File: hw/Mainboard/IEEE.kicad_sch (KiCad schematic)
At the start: 26 parts, among them J10 IEEE_HEADER, J11 IEEE, U14 74LS245, U15 SN74LS07, U16 SN74LS07, U17 74LS245, U18 SN74LS07

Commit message: hw: 25x2 header (wip)
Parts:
- renumbered J10 to J11, J11 to J12
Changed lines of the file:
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@@
   (symbol (lib_id "Retrocomputing:CBM_PET_IEEE_Conn_02x12_Card_Edge") (at 238.76 119.38 0) (unit 1)
     (in_bom yes) (on_board yes)
-    (property "Reference" "J11" (id 0) (at 240.03 101.1682 0))
+    (property "Reference" "J12" (id 0) (at 240.03 101.1682 0))
     (property "Value" "IEEE" (id 1) (at 240.03 103.4796 0))
     (property "Footprint" "Retrocomputing:CBM_PET_IEEE_EDGE_CON_24P" (id 2) (at 238.76 119.38 0)
@@
   (symbol (lib_id "PET:PD_GND") (at 204.47 44.45 0) (unit 1)
     (in_bom yes) (on_board yes) (fields_autoplaced)
-    (property "Reference" "#PWR090" (id 0) (at 204.47 50.8 0)
+    (property "Reference" "#PWR092" (id 0) (at 204.47 50.8 0)
       (effects (font (size 1.27 1.27)) hide)
     )
@@
   (symbol (lib_id "power:GND") (at 194.31 147.32 0) (unit 1)
     (in_bom yes) (on_board yes)
-    (property "Reference" "#PWR099" (id 0) (at 194.31 153.67 0)
+    (property "Reference" "#PWR0101" (id 0) (at 194.31 153.67 0)
       (effects (font (size 1.27 1.27)) hide)
     )
@@
   (symbol (lib_id "Connector_Generic:Conn_02x09_Odd_Even") (at 210.82 34.29 0) (mirror x) (unit 1)
     (in_bom yes) (on_board yes) (fields_autoplaced)
-    (property "Reference" "J10" (id 0) (at 212.09 17.78 0))
+    (property "Reference" "J11" (id 0) (at 212.09 17.78 0))
     (property "Value" "IEEE_HEADER" (id 1) (at 212.09 20.32 0))
     (property "Footprint" "Connector_PinHeader_2.54mm:PinHeader_2x09_P2.54mm_Vertical" (id 2) (at 210.82 34.29 0)
@@
   (symbol (lib_id "power:+5V") (at 67.31 130.81 0) (unit 1)
     (in_bom yes) (on_board yes) (fields_autoplaced)
-    (property "Reference" "#PWR095" (id 0) (at 67.31 134.62 0)
+    (property "Reference" "#PWR097" (id 0) (at 67.31 134.62 0)
       (effects (font (size 1.27 1.27)) hide)
     )
@@
   (symbol (lib_id "power:GND") (at 128.27 71.12 0) (unit 1)
     (in_bom yes) (on_board yes)
-    (property "Reference" "#PWR093" (id 0) (at 128.27 77.47 0)
+    (property "Reference" "#PWR095" (id 0) (at 128.27 77.47 0)
       (effects (font (size 1.27 1.27)) hide)
     )
@@
   (symbol (lib_id "PET:PD_GND") (at 219.71 44.45 0) (unit 1)
     (in_bom yes) (on_board yes) (fields_autoplaced)
-    (property "Reference" "#PWR091" (id 0) (at 219.71 50.8 0)
+    (property "Reference" "#PWR093" (id 0) (at 219.71 50.8 0)
       (effects (font (size 1.27 1.27)) hide)
     )
@@
   (symbol (lib_id "PET:PD_GND") (at 247.65 135.89 0) (unit 1)
     (in_bom yes) (on_board yes) (fields_autoplaced)
-    (property "Reference" "#PWR097" (id 0) (at 247.65 142.24 0)
+    (property "Reference" "#PWR099" (id 0) (at 247.65 142.24 0)
       (effects (font (size 1.27 1.27)) hide)
     )
@@
   (symbol (lib_id "power:GND") (at 64.77 193.04 0) (unit 1)
     (in_bom yes) (on_board yes)
-    (property "Reference" "#PWR0101" (id 0) (at 64.77 199.39 0)
+    (property "Reference" "#PWR0103" (id 0) (at 64.77 199.39 0)
       (effects (font (size 1.27 1.27)) hide)
     )
@@
   (symbol (lib_id "power:GND") (at 128.27 182.88 0) (unit 1)
     (in_bom yes) (on_board yes)
-    (property "Reference" "#PWR0100" (id 0) (at 128.27 189.23 0)
+    (property "Reference" "#PWR0102" (id 0) (at 128.27 189.23 0)
       (effects (font (size 1.27 1.27)) hide)
     )
@@
   (symbol (lib_id "power:GND") (at 55.88 143.51 0) (unit 1)
     (in_bom yes) (on_board yes)
-    (property "Reference" "#PWR098" (id 0) (at 55.88 149.86 0)
+    (property "Reference" "#PWR0100" (id 0) (at 55.88 149.86 0)
       (effects (font (size 1.27 1.27)) hide)
     )
@@
   (symbol (lib_id "power:GND") (at 64.77 113.03 0) (unit 1)
     (in_bom yes) (on_board yes)
-    (property "Reference" "#PWR094" (id 0) (at 64.77 119.38 0)
+    (property "Reference" "#PWR096" (id 0) (at 64.77 119.38 0)
       (effects (font (size 1.27 1.27)) hide)
     )
@@
   (symbol (lib_id "PET:CHASSIS_GND") (at 232.41 135.89 0) (unit 1)
     (in_bom yes) (on_board yes)
-    (property "Reference" "#PWR096" (id 0) (at 232.41 140.97 0)
+    (property "Reference" "#PWR098" (id 0) (at 232.41 140.97 0)
       (effects (font (size 1.27 1.27)) hide)
     )
@@
   (symbol (lib_id "power:GND") (at 64.77 67.31 0) (unit 1)
     (in_bom yes) (on_board yes)
-    (property "Reference" "#PWR092" (id 0) (at 64.77 73.66 0)
-      (effects (font (size 1.27 1.27)) hide)
-    )
+    (property "Reference" "#PWR094" (id 0) (at 64.77 73.66 0)
+      (effects (font (size 1.27 1.27)) hide)
+    )

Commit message: hw: 2x config switch (wip)
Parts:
- renumbered J11 to J10, J12 to J11
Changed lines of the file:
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@@
   (symbol (lib_id "Retrocomputing:CBM_PET_IEEE_Conn_02x12_Card_Edge") (at 238.76 119.38 0) (unit 1)
     (in_bom yes) (on_board yes)
-    (property "Reference" "J12" (id 0) (at 240.03 101.1682 0))
+    (property "Reference" "J11" (id 0) (at 240.03 101.1682 0))
     (property "Value" "IEEE" (id 1) (at 240.03 103.4796 0))
     (property "Footprint" "Retrocomputing:CBM_PET_IEEE_EDGE_CON_24P" (id 2) (at 238.76 119.38 0)
@@
   (symbol (lib_id "PET:PD_GND") (at 204.47 44.45 0) (unit 1)
     (in_bom yes) (on_board yes) (fields_autoplaced)
-    (property "Reference" "#PWR092" (id 0) (at 204.47 50.8 0)
+    (property "Reference" "#PWR098" (id 0) (at 204.47 50.8 0)
       (effects (font (size 1.27 1.27)) hide)
     )
@@
   (symbol (lib_id "power:GND") (at 194.31 147.32 0) (unit 1)
     (in_bom yes) (on_board yes)
-    (property "Reference" "#PWR0101" (id 0) (at 194.31 153.67 0)
+    (property "Reference" "#PWR0107" (id 0) (at 194.31 153.67 0)
       (effects (font (size 1.27 1.27)) hide)
     )
@@
   (symbol (lib_id "Connector_Generic:Conn_02x09_Odd_Even") (at 210.82 34.29 0) (mirror x) (unit 1)
     (in_bom yes) (on_board yes) (fields_autoplaced)
-    (property "Reference" "J11" (id 0) (at 212.09 17.78 0))
+    (property "Reference" "J10" (id 0) (at 212.09 17.78 0))
     (property "Value" "IEEE_HEADER" (id 1) (at 212.09 20.32 0))
     (property "Footprint" "Connector_PinHeader_2.54mm:PinHeader_2x09_P2.54mm_Vertical" (id 2) (at 210.82 34.29 0)
@@
   (symbol (lib_id "power:+5V") (at 67.31 130.81 0) (unit 1)
     (in_bom yes) (on_board yes) (fields_autoplaced)
-    (property "Reference" "#PWR097" (id 0) (at 67.31 134.62 0)
+    (property "Reference" "#PWR0103" (id 0) (at 67.31 134.62 0)
       (effects (font (size 1.27 1.27)) hide)
     )
@@
   (symbol (lib_id "power:GND") (at 128.27 71.12 0) (unit 1)
     (in_bom yes) (on_board yes)
-    (property "Reference" "#PWR095" (id 0) (at 128.27 77.47 0)
+    (property "Reference" "#PWR0101" (id 0) (at 128.27 77.47 0)
       (effects (font (size 1.27 1.27)) hide)
     )
@@
   (symbol (lib_id "PET:PD_GND") (at 219.71 44.45 0) (unit 1)
     (in_bom yes) (on_board yes) (fields_autoplaced)
-    (property "Reference" "#PWR093" (id 0) (at 219.71 50.8 0)
+    (property "Reference" "#PWR099" (id 0) (at 219.71 50.8 0)
       (effects (font (size 1.27 1.27)) hide)
     )
@@
   (symbol (lib_id "PET:PD_GND") (at 247.65 135.89 0) (unit 1)
     (in_bom yes) (on_board yes) (fields_autoplaced)
-    (property "Reference" "#PWR099" (id 0) (at 247.65 142.24 0)
+    (property "Reference" "#PWR0105" (id 0) (at 247.65 142.24 0)
       (effects (font (size 1.27 1.27)) hide)
     )
@@
   (symbol (lib_id "power:GND") (at 64.77 193.04 0) (unit 1)
     (in_bom yes) (on_board yes)
-    (property "Reference" "#PWR0103" (id 0) (at 64.77 199.39 0)
+    (property "Reference" "#PWR0109" (id 0) (at 64.77 199.39 0)
       (effects (font (size 1.27 1.27)) hide)
     )
@@
   (symbol (lib_id "power:GND") (at 128.27 182.88 0) (unit 1)
     (in_bom yes) (on_board yes)
-    (property "Reference" "#PWR0102" (id 0) (at 128.27 189.23 0)
+    (property "Reference" "#PWR0108" (id 0) (at 128.27 189.23 0)
       (effects (font (size 1.27 1.27)) hide)
     )
@@
   (symbol (lib_id "power:GND") (at 55.88 143.51 0) (unit 1)
     (in_bom yes) (on_board yes)
-    (property "Reference" "#PWR0100" (id 0) (at 55.88 149.86 0)
+    (property "Reference" "#PWR0106" (id 0) (at 55.88 149.86 0)
       (effects (font (size 1.27 1.27)) hide)
     )
@@
   (symbol (lib_id "power:GND") (at 64.77 113.03 0) (unit 1)
     (in_bom yes) (on_board yes)
-    (property "Reference" "#PWR096" (id 0) (at 64.77 119.38 0)
+    (property "Reference" "#PWR0102" (id 0) (at 64.77 119.38 0)
       (effects (font (size 1.27 1.27)) hide)
     )
@@
   (symbol (lib_id "PET:CHASSIS_GND") (at 232.41 135.89 0) (unit 1)
     (in_bom yes) (on_board yes)
-    (property "Reference" "#PWR098" (id 0) (at 232.41 140.97 0)
+    (property "Reference" "#PWR0104" (id 0) (at 232.41 140.97 0)
       (effects (font (size 1.27 1.27)) hide)
     )
@@
   (symbol (lib_id "power:GND") (at 64.77 67.31 0) (unit 1)
     (in_bom yes) (on_board yes)
-    (property "Reference" "#PWR094" (id 0) (at 64.77 73.66 0)
-      (effects (font (size 1.27 1.27)) hide)
-    )
+    (property "Reference" "#PWR0100" (id 0) (at 64.77 73.66 0)
+      (effects (font (size 1.27 1.27)) hide)
+    )

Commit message: hw: touchups (wip)
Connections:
- net VCC is gone; now on net +5V: C57.1, C58.1, C59.1, C60.1, C61.1, J10.4 (Pin_4), PT36.2, RN5.5 (R4.2), RN5.6 (R3.2), RN5.7 (R2.2), RN5.8 (R1.2), RN6.5 (R4.2), RN6.6 (R3.2), RN6.7 (R2.2), RN6.8 (R1.2), RN7.5 (R4.2), RN7.6 (R3.2), RN7.7 (R2.2), RN7.8 (R1.2), RN8.5 (R4.2), RN8.6 (R3.2), RN8.7 (R2.2), RN8.8 (R1.2), U14.1 (A->B), U14.20 (VCC), U15.14 (VCC), U16.14 (VCC), U17.1 (A->B), U17.20 (VCC), U18.14 (VCC)
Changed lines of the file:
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@@
   (junction (at 64.77 67.31) (diameter 0) (color 0 0 0 0)
   )
+  (junction (at 60.96 130.81) (diameter 0) (color 0 0 0 0)
+  )
   (junction (at 50.8 101.6) (diameter 0) (color 0 0 0 0)
   )
@@
   )
   (junction (at 205.74 146.05) (diameter 0) (color 0 0 0 0)
+  )
+  (junction (at 66.04 130.81) (diameter 0) (color 0 0 0 0)
   )
   (junction (at 200.66 146.05) (diameter 0) (color 0 0 0 0)
@@
     (stroke (width 0) (type default) (color 0 0 0 0))
   )
+  (wire (pts (xy 60.96 130.81) (xy 66.04 130.81))
+    (stroke (width 0) (type default) (color 0 0 0 0))
+  )

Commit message: hw: caps & logos (wip)
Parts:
- added C102: 1u, Capacitor_SMD:C_0402_1005Metric, symbol Device:C_Small
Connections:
- net +5V: now also C102.1
- net PD_GND: now also C102.2
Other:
- title: CBM PET Mainboard Replacement -> EconoPET 40/8096
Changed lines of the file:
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@@
   (paper "A")
   (title_block
-    (title "CBM PET Mainboard Replacement")
+    (title "EconoPET 40/8096")
+    (date "2023-10-01")
+    (rev "A")
   )
   (bus_alias "IEEE_IN" (members "DAV_IN" "NRFD_IN" "NDAC_IN" "ATN_IN" "EOI_IN" "SRQ_IN"))
@@
   (junction (at 203.2 72.39) (diameter 0) (color 0 0 0 0)
   )
+  (junction (at 212.09 49.53) (diameter 0) (color 0 0 0 0)
+  )
   (junction (at 219.71 72.39) (diameter 0) (color 0 0 0 0)
   )
@@
   )
   (junction (at 194.31 146.05) (diameter 0) (color 0 0 0 0)
+  )
+  (junction (at 219.71 49.53) (diameter 0) (color 0 0 0 0)
   )
   (junction (at 186.69 72.39) (diameter 0) (color 0 0 0 0)
@@
     (stroke (width 0) (type default) (color 0 0 0 0))
   )
+  (wire (pts (xy 228.6 41.91) (xy 228.6 43.18))
+    (stroke (width 0) (type default) (color 0 0 0 0))
+  )
   (wire (pts (xy 114.3 154.94) (xy 115.57 154.94))
     (stroke (width 0) (type default) (color 0 0 0 0))
@@
     (stroke (width 0) (type default) (color 0 0 0 0))
   )
+  (wire (pts (xy 212.09 49.53) (xy 219.71 49.53))
+    (stroke (width 0) (type default) (color 0 0 0 0))
+  )
   (wire (pts (xy 261.62 88.9) (xy 198.12 88.9))
     (stroke (width 0) (type default) (color 0 0 0 0))
@@
     (stroke (width 0) (type default) (color 0 0 0 0))
   )
+  (wire (pts (xy 204.47 49.53) (xy 204.47 44.45))
+    (stroke (width 0) (type default) (color 0 0 0 0))
+  )
+  (wire (pts (xy 228.6 48.26) (xy 228.6 49.53))
+    (stroke (width 0) (type default) (color 0 0 0 0))
+  )
   (bus (pts (xy 154.94 86.36) (xy 154.94 88.9))
     (stroke (width 0) (type default) (color 0 0 0 0))
@@
     (stroke (width 0) (type default) (color 0 0 0 0))
   )
-  (wire (pts (xy 218.44 41.91) (xy 222.25 41.91))
+  (wire (pts (xy 218.44 41.91) (xy 228.6 41.91))
     (stroke (width 0) (type default) (color 0 0 0 0))
   )
@@
     (stroke (width 0) (type default) (color 0 0 0 0))
   )
+  (wire (pts (xy 212.09 49.53) (xy 204.47 49.53))
+    (stroke (width 0) (type default) (color 0 0 0 0))
+  )
   (wire (pts (xy 140.97 48.26) (xy 152.4 48.26))
     (stroke (width 0) (type default) (color 0 0 0 0))
@@
     (stroke (width 0) (type default) (color 0 0 0 0))
   )
+  (wire (pts (xy 219.71 44.45) (xy 219.71 49.53))
+    (stroke (width 0) (type default) (color 0 0 0 0))
+  )
   (wire (pts (xy 55.88 143.51) (xy 55.88 142.24))
     (stroke (width 0) (type default) (color 0 0 0 0))
@@
   )
   (wire (pts (xy 194.31 146.05) (xy 198.12 146.05))
+    (stroke (width 0) (type default) (color 0 0 0 0))
+  )
+  (wire (pts (xy 219.71 49.53) (xy 228.6 49.53))
     (stroke (width 0) (type default) (color 0 0 0 0))
   )
@@
     (pin "8")
   )
-  (symbol (lib_id "PET:PD_GND") (at 204.47 44.45 0) (unit 1)
-    (in_bom yes) (on_board yes) (fields_autoplaced)
-    (property "Reference" "#PWR098" (id 0) (at 204.47 50.8 0)
-      (effects (font (size 1.27 1.27)) hide)
-    )
-    (property "Value" "PD_GND" (id 1) (at 204.47 49.53 0))
-    (property "Footprint" "" (id 2) (at 204.47 44.45 0)
-      (effects (font (size 1.27 1.27)) hide)
-    )
-    (property "Datasheet" "" (id 3) (at 204.47 44.45 0)
-      (effects (font (size 1.27 1.27)) hide)
-    )
-    (pin "1")
-  )
   (symbol (lib_id "power:GND") (at 194.31 147.32 0) (unit 1)
     (in_bom yes) (on_board yes)
@@
     (pin "8")
   )
+  (symbol (lib_id "Device:C_Small") (at 228.6 45.72 0) (unit 1)
+    (in_bom yes) (on_board yes)
+    (property "Reference" "C102" (id 0) (at 230.9368 44.5516 0)
+      (effects (font (size 1.27 1.27)) (justify left))
+    )
+    (property "Value" "1u" (id 1) (at 230.9368 46.863 0)
+      (effects (font (size 1.27 1.27)) (justify left))
+    )
+    (property "Footprint" "Capacitor_SMD:C_0402_1005Metric" (id 2) (at 228.6 45.72 0)
+      (effects (font (size 1.27 1.27)) hide)
+    )
+    (property "Datasheet" "https://datasheet.lcsc.com/lcsc/2304140030_Samsung-Electro-Mechanics-CL05A105KA5NQNC_C52923.pdf" (id 3) (at 228.6 45.72 0)
+      (effects (font (size 1.27 1.27)) hide)
+    )
+    (property "LCSC" "C52923" (id 4) (at 228.6 45.72 0)
+      (effects (font (size 1.27 1.27)) hide)
+    )
+    (pin "1")
+    (pin "2")
+  )
   (symbol (lib_id "power:GND") (at 128.27 71.12 0) (unit 1)
     (in_bom yes) (on_board yes)
@@
     (pin "8")
   )
-  (symbol (lib_id "PET:PD_GND") (at 219.71 44.45 0) (unit 1)
+  (symbol (lib_id "PET:PD_GND") (at 212.09 49.53 0) (unit 1)
     (in_bom yes) (on_board yes) (fields_autoplaced)
-    (property "Reference" "#PWR099" (id 0) (at 219.71 50.8 0)
-      (effects (font (size 1.27 1.27)) hide)
-    )
-    (property "Value" "PD_GND" (id 1) (at 219.71 49.53 0))
-    (property "Footprint" "" (id 2) (at 219.71 44.45 0)
-      (effects (font (size 1.27 1.27)) hide)
-    )
-    (property "Datasheet" "" (id 3) (at 219.71 44.45 0)
-      (effects (font (size 1.27 1.27)) hide)
-    )
+    (property "Reference" "#PWR099" (id 0) (at 212.09 55.88 0)
+      (effects (font (size 1.27 1.27)) hide)
+    )
+    (property "Value" "PD_GND" (id 1) (at 212.09 54.61 0))
+    (property "Footprint" "" (id 2) (at 212.09 49.53 0)
+      (effects (font (size 1.27 1.27)) hide)
+    )
+    (property "Datasheet" "" (id 3) (at 212.09 49.53 0)
+      (effects (font (size 1.27 1.27)) hide)
+    )

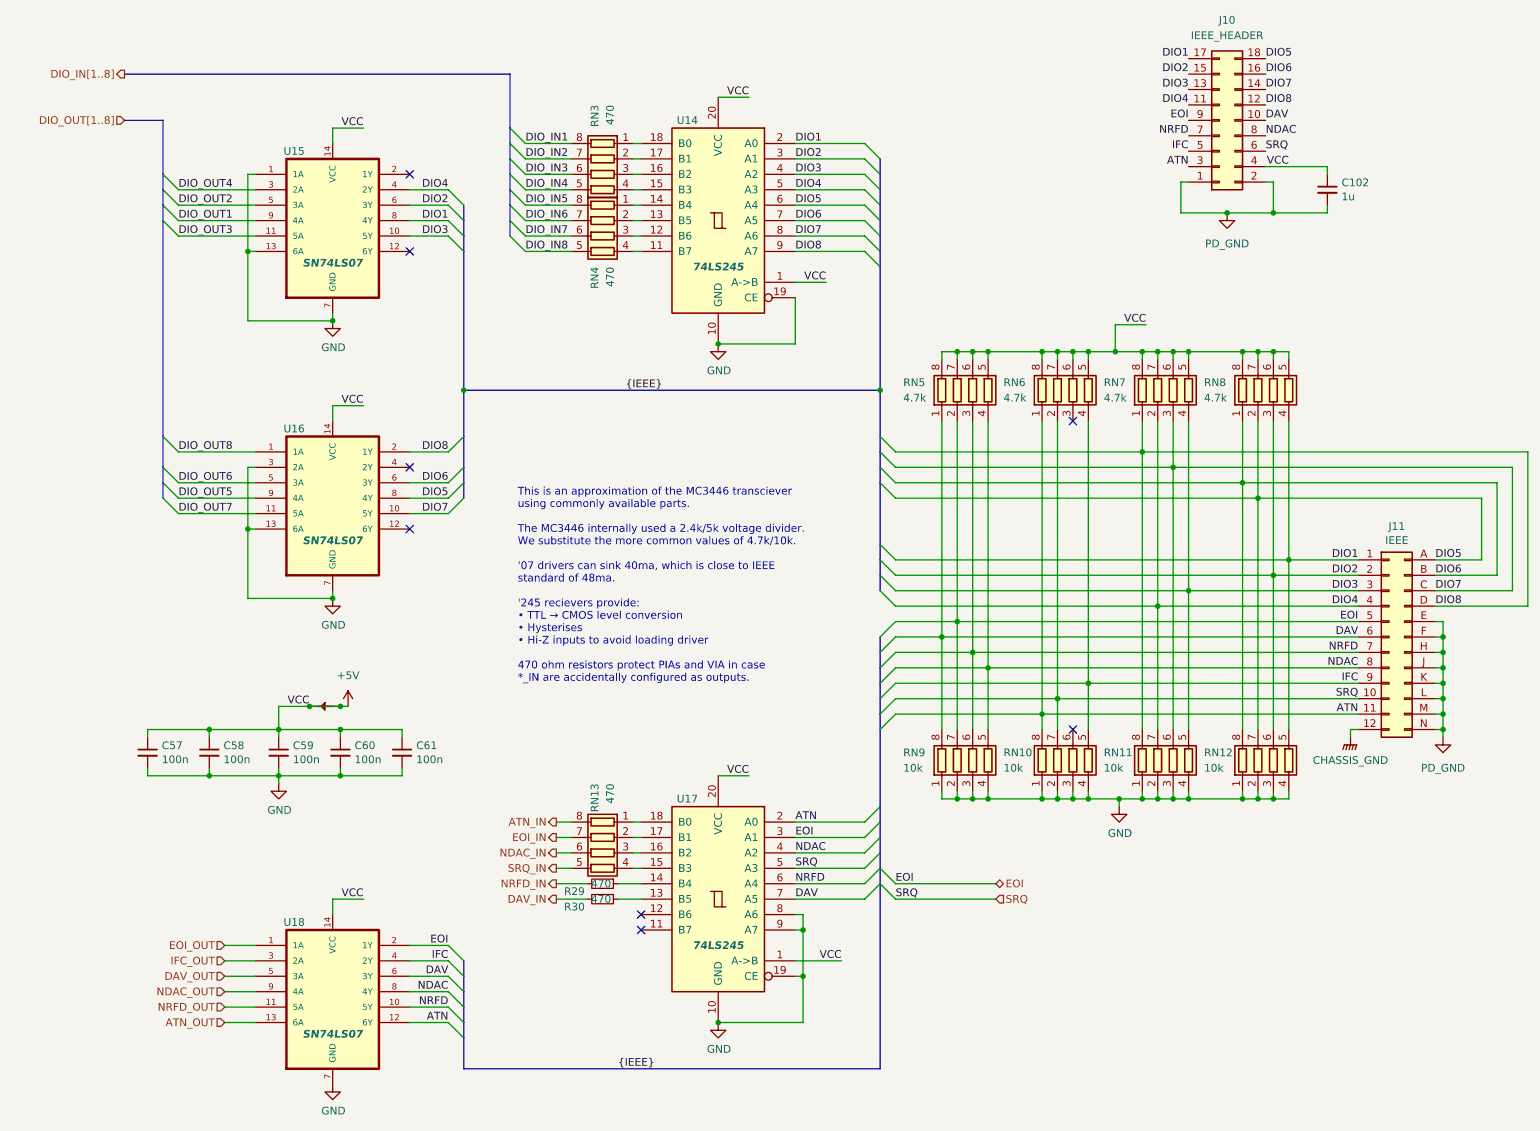
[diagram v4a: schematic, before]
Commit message: hw: remove net/power ties
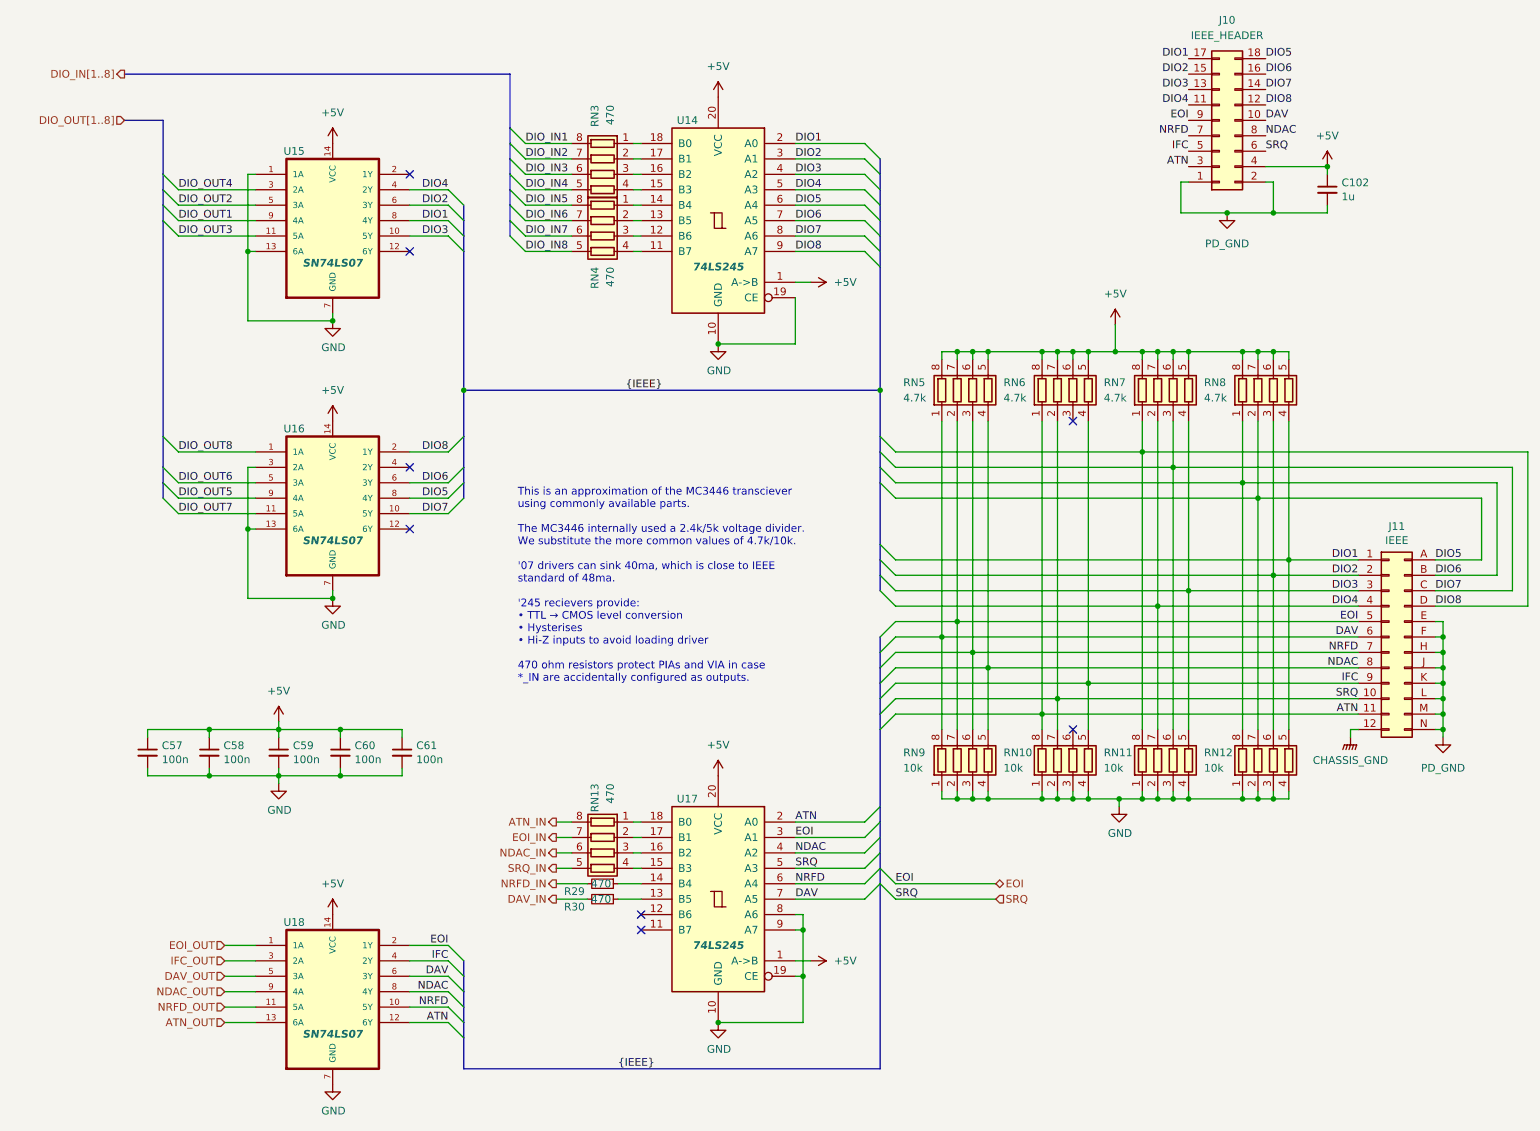
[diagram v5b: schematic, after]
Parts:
- removed PT36: PowerTie_2, PET:NetTie-2_SMD_Pad_1.6_to_0.4mm, symbol PET:PowerTie_2
